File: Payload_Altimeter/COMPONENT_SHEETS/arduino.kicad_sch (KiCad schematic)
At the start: 1 part, among them U1 Arduino_Pro_Mini

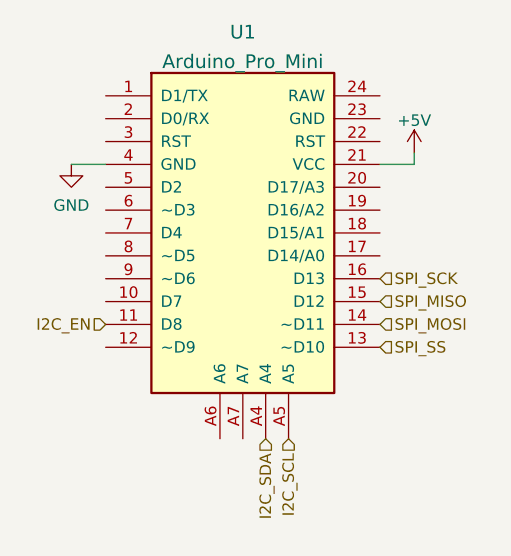
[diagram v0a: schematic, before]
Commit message: added sd card
sd card was added and traces were placed for other components
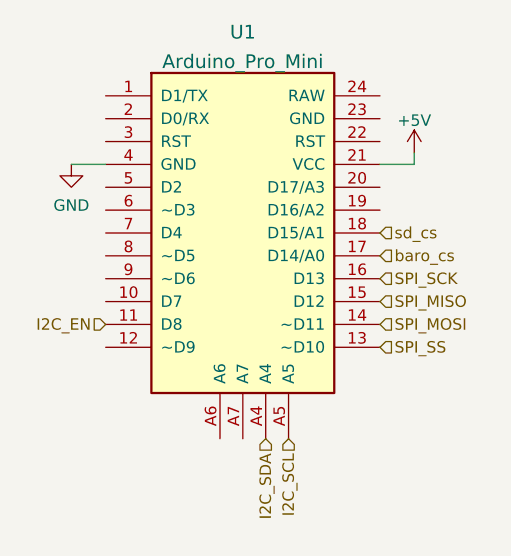
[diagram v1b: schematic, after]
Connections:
- net baro_cs: now reaches U1.17 (D14/A0)
- net sd_cs: now reaches U1.18 (D15/A1)
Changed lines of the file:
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@@
     (effects (font (size 1.27 1.27)) (justify right))
+  )
+  (hierarchical_label "baro_cs" (shape input) (at 152.4 87.63 0)
+    (effects (font (size 1.27 1.27)) (justify left))
   )
   (hierarchical_label "I2C_SCL" (shape input) (at 142.24 107.95 270)
@@
     (effects (font (size 1.27 1.27)) (justify left))
   )
+  (hierarchical_label "sd_cs" (shape input) (at 152.4 85.09 0)
+    (effects (font (size 1.27 1.27)) (justify left))
+  )
